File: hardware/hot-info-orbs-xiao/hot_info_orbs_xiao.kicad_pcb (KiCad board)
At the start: 2 copper layers, 198.8 x 28.5 mm, 11 parts, among them SW1 SW_Push, SW2 SW_Push, SW3 SW_Push, U2 ESP32-S3-SuperMini

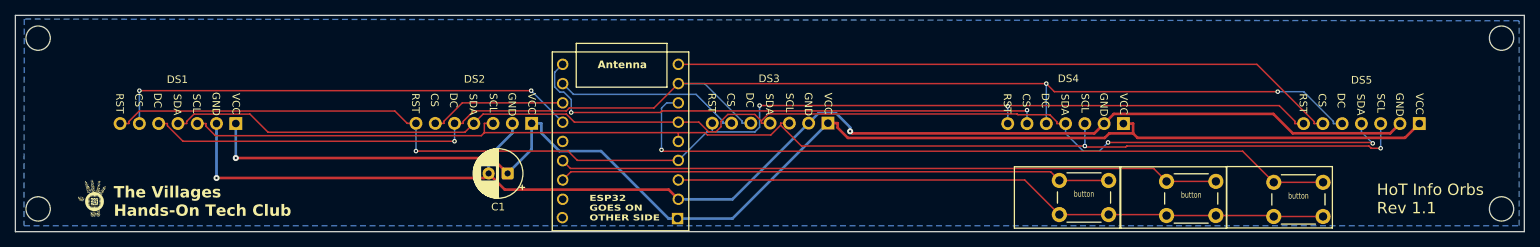
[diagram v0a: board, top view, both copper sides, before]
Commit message: xiao: schematic + PCB swap scripts, first run (WIP checkpoint)
Schematic: SuperMini symbol out, XIAO U2 in with net labels per the pin
map, R1/C2 RC reset on /RST, ERC clean. PCB: XIAO-ESP32-S3-DIP on B.Cu,
R1/C2 on F.Cu, every pad re-netted, tracks ripped. Scripts already carry
the DRC fixes (FPID, Description, 14-pin symbol, U2 y 95, silk) but the
.kicad_sch/.kicad_pcb here are from the run BEFORE those fixes — next
commit reruns both from e6ea813. Committed mid-stream on purpose so a
model switch loses nothing.

Co-Authored-By: Claude Fable 5.1 <noreply@anthropic.com>
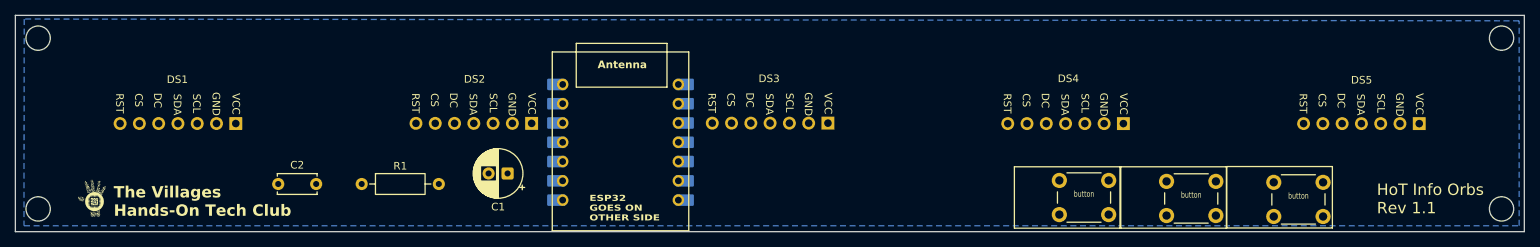
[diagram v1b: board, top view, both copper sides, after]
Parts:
- added C2: 1u, C_Disc_D5.0mm_W2.5mm_P5.00mm, F.Cu at (86.0, 101.5)
- added R1: 10k, R_Axial_DIN0207_L6.3mm_D2.5mm_P10.16mm_Horizontal, F.Cu at (97.0, 101.5)
- U2: value ESP32-S3-SuperMini -> XIAO ESP32-S3 Plus; footprint _ESP32 modules:ESP32S3-SuperMini -> XIAO-ESP32-S3-DIP
- moved U2 0.11 mm to (131.1, 96.0), turned to -90 degrees
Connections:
- DS1 pad 3: Net-(DS1-SCL) -> /SCLK
- DS1 pad 4: Net-(DS1-SDA) -> /MOSI
- DS1 pad 5: Net-(DS1-DC) -> /DC
- DS1 pad 6: Net-(DS1-CS) -> /CS1
- DS1 pad 7: Net-(DS1-RST) -> /RST
- DS2 pad 3: Net-(DS1-SCL) -> /SCLK
- DS2 pad 4: Net-(DS1-SDA) -> /MOSI
- DS2 pad 5: Net-(DS1-DC) -> /DC
- DS2 pad 6: Net-(DS2-CS) -> /CS2
- DS2 pad 7: Net-(DS1-RST) -> /RST
- DS3 pad 3: Net-(DS1-SCL) -> /SCLK
- DS3 pad 4: Net-(DS1-SDA) -> /MOSI
- DS3 pad 5: Net-(DS1-DC) -> /DC
- DS3 pad 6: Net-(DS3-CS) -> /CS3
- DS3 pad 7: Net-(DS1-RST) -> /RST
- DS4 pad 3: Net-(DS1-SCL) -> /SCLK
- DS4 pad 4: Net-(DS1-SDA) -> /MOSI
- DS4 pad 5: Net-(DS1-DC) -> /DC
- DS4 pad 6: Net-(DS4-CS) -> /CS4
- DS4 pad 7: Net-(DS1-RST) -> /RST
- DS5 pad 3: Net-(DS1-SCL) -> /SCLK
- DS5 pad 4: Net-(DS1-SDA) -> /MOSI
- DS5 pad 5: Net-(DS1-DC) -> /DC
- DS5 pad 6: Net-(DS5-CS) -> /CS5
- DS5 pad 7: Net-(DS1-RST) -> /RST
- SW1 pad 1: Net-(U2-GPIO_1) -> /SW1
- SW1 pad 2: Net-(U2-3V3) -> /3V3
- SW2 pad 1: Net-(U2-GPIO_2) -> /SW2
- SW2 pad 2: Net-(U2-3V3) -> /3V3
- SW3 pad 2: Net-(U2-3V3) -> /3V3
- U2 pad 1: +5V -> /SW1
- U2 pad 10: Net-(DS4-CS) -> /DC
- U2 pad 11: Net-(DS3-CS) -> /MOSI
- U2 pad 12: Net-(DS2-CS) -> /3V3
- U2 pad 13: Net-(DS1-CS) -> GND
- U2 pad 14: unconnected-(U2-GPIO_3-Pad14) -> +5V
- U2 pad 2: GND -> /SW2
- U2 pad 3: Net-(U2-3V3) -> /CS1
- U2 pad 4: Net-(DS1-RST) -> /CS2
- U2 pad 5: Net-(DS1-SCL) -> /CS3
- U2 pad 6: Net-(DS1-SDA) -> /SW3
- U2 pad 7: /SW3 -> /CS4
- U2 pad 8: Net-(DS1-DC) -> /CS5
- U2 pad 9: Net-(DS5-CS) -> /SCLK
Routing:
- net +5V: track 182.2 -> 0.00 mm, vias 1 -> 0
- net GND: track 181.4 -> 0.00 mm, vias 2 -> 0
- net Net-(DS1-DC): track 181.2 -> 0.00 mm, vias 3 -> 0
- net Net-(DS1-SDA): track 171.3 -> 0.00 mm, vias 2 -> 0
- net Net-(DS1-RST): track 171.0 -> 0.00 mm, vias 3 -> 0
- net Net-(DS1-SCL): track 170.2 -> 0.00 mm, vias 2 -> 0
- net /SW3: track 96.9 -> 0.00 mm, vias 1 -> 0
- net Net-(DS5-CS): track 88.3 -> 0.00 mm
- net Net-(U2-GPIO_2): track 87.2 -> 0.00 mm
- net Net-(U2-3V3): track 86.9 -> 0.00 mm
- net Net-(U2-GPIO_1): track 72.9 -> 0.00 mm
- net Net-(DS4-CS): track 70.0 -> 0.00 mm, vias 2 -> 0
- net Net-(DS1-CS): track 61.8 -> 0.00 mm, vias 2 -> 0
- net Net-(DS3-CS): track 24.6 -> 0.00 mm
- net Net-(DS2-CS): track 18.1 -> 0.00 mm

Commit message: xiao: schematic + PCB regenerated from e6ea813, DRC/parity clean before routing
Both swap scripts rerun against the untouched copy so the result is
reproducible rather than hand-patched. Symbol trimmed to the 14 edge pins
(renamed XIAO-ESP32-S3-edge) instead of carrying 11 no_connects that
parity flagged as pad-less. U2 moved to y 95.0 so the 21 mm module stays
inside the 107.8 edge; SuperMini silk art rewritten for the XIAO; the
B.Silk keepout rectangle removed (rule area kept). Description copied
via GetField().SetText() — SetField(FIELD_T_DESCRIPTION) makes a stray
field '5' that printed on silk and produced 134 bogus warnings.

DRC: 0 errors, 0 parity, 45 unconnected (not yet routed), 14 accepted
warnings = Seeed outline over its own castellations.

Co-Authored-By: Claude Fable 5.1 <noreply@anthropic.com>
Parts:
- C2: footprint C_Disc_D5.0mm_W2.5mm_P5.00mm -> Capacitor_THT:C_Disc_D5.0mm_W2.5mm_P5.00mm
- R1: footprint R_Axial_DIN0207_L6.3mm_D2.5mm_P10.16mm_Horizontal -> Resistor_THT:R_Axial_DIN0207_L6.3mm_D2.5mm_P10.16mm_Horizontal
- U2: footprint XIAO-ESP32-S3-DIP -> _ESP32 modules:XIAO-ESP32-S3-DIP
- moved U2 1.00 mm to (131.1, 95.0)
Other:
- board text added: "HoT Info Orbs XIAO X0.1"
- board text added: "XIAO GOES ON OTHER SIDE"
- board text added: "XIAO GOES ON THIS SIDE"
- board text removed: "ESP32 GOES ON OTHER SIDE"
- board text removed: "ESP32 GOES ON THIS SIDE"
- board text removed: "HoT Info Orbs Rev 1.1"

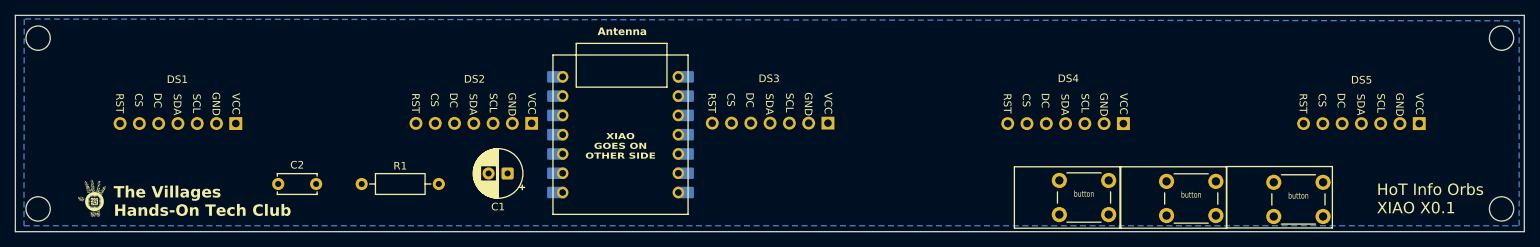
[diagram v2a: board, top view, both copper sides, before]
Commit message: xiao: autorouted, DRC 0 errors / 0 unconnected / parity clean
Freerouting runs headless from tools/route_xiao.py (DSN out, SES in,
DRC with zone refill). Two things had to change for it to finish:

- The GND pour is left out of the DSN. With it, Freerouting treats GND
  as a plane and routes nothing, and the new tracks slice the pour into
  islands (3 starved thermals, 2 unconnected). GND is now routed as
  tracks and the pour is refilled on top.
- Seeed's footprint has two pads per pin (PTH + castellation SMD).
  Freerouting counted the 14 overlaps as violations, stubbed every pin
  and left one net unrouted each run — CS4, then MOSI once CS4 was
  pre-routed by hand, so hand-routing was rejected. merge_xiao_pads.py
  makes each pin one oval THT pad (hole stays at +-7.62, copper to
  +-9.671): 0 violations, 0 unrouted, and one piece of copper for both
  header and castellation builds.

Remaining 14 warnings are Seeed's own silk outline over its pads.
Scripts carry the pcbnew SWIG traps (one board per process, zones
before tracks, GetField not SetField for Description).

Co-Authored-By: Claude Fable 5.1 <noreply@anthropic.com>
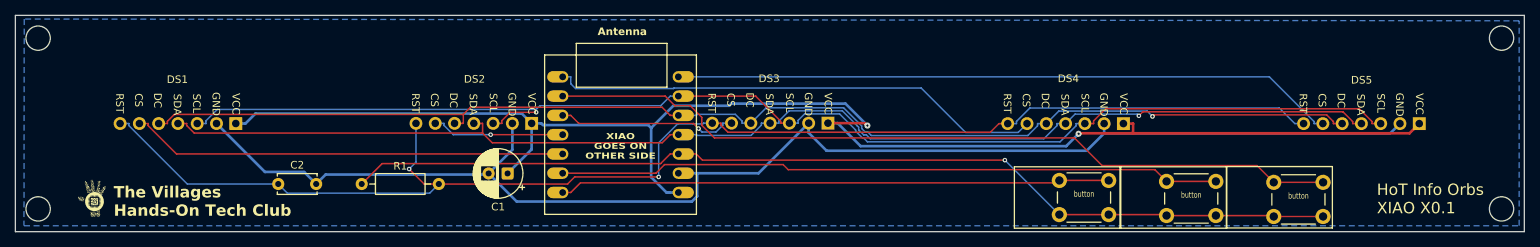
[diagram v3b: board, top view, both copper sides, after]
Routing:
- net +5V: track 0.00 -> 194.2 mm, vias 0 -> 2
- net GND: track 0.00 -> 182.8 mm
- net /RST: track 0.00 -> 180.5 mm, vias 0 -> 2
- net /SCLK: track 0.00 -> 171.6 mm, vias 0 -> 1
- net /MOSI: track 0.00 -> 166.1 mm, vias 0 -> 1
- net /DC: track 0.00 -> 165.5 mm, vias 0 -> 1
- net /3V3: track 0.00 -> 131.7 mm, vias 0 -> 1
- net /SW3: track 0.00 -> 105.5 mm
- net /CS5: track 0.00 -> 87.6 mm
- net /SW2: track 0.00 -> 87.5 mm
- net /SW1: track 0.00 -> 72.6 mm
- net /CS4: track 0.00 -> 65.3 mm
- net /CS1: track 0.00 -> 57.6 mm
- net /CS3: track 0.00 -> 23.8 mm, vias 0 -> 1
- net /CS2: track 0.00 -> 17.6 mm, vias 0 -> 1

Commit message: xiao board: copper-free 40 x 7.5 mm patch for the FPC antenna, SuperMini keepouts removed
The XIAO ESP32-S3 / S3 Plus has a U.FL and a stick-on FPC antenna (Seeed
A-02), not a PCB antenna, so the inherited "Antenna" keepouts and silk were
leftovers. tools/antenna_patch.py replaces them with rule area ANTENNA_PATCH
(no pour/tracks/vias, F.Cu + B.Cu) at x 143.5-183.5, y 99.5-107.0 on the
back right of the XIAO, with a B.Silk box and label. Board re-routed:
0 DRC errors, 0 unconnected, 0 parity, pour has no fill inside the patch.

Why 7.5 mm tall and not the 10.5 mm the strip offers: that strip is the SPI
bus's second channel to DS4/DS5 and the switches. Measured against
Freerouting (20 passes, -mt 1): 10.5 mm -> 3 nets unrouted, 9.0 mm -> CS2
unrouted, 7.5 mm -> clean. Narrowing instead (x from 150 or 155) still left
a net unrouted; x 160.5-183.5 routes at 10.5 mm but is only 23 mm long.
Allowing tracks on F.Cu inside the patch was rejected: copper 1.6 mm behind
a flex antenna still detunes it, and the router does not need the space.

The size is an assumption: Seeed publishes no A-02 dimensions. Measure one
and rerun with PATCH=x0,x1,y0,y1 before ordering boards.

route_xiao.py: -mt 1 (Freerouting 2.4.1 warns its multi-threaded optimizer
is broken) and an assert on SES size - Freerouting writes a 0-byte SES when
nets are left unrouted, and the import then failed with no hint.

Co-Authored-By: Claude Fable 5.1 <noreply@anthropic.com>
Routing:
- net /RST: track 180.5 -> 202.3 mm, vias 2 -> 0
- net /DC: track 165.5 -> 178.5 mm
- net +5V: track 194.2 -> 182.2 mm, vias 2 -> 0
- net /SCLK: track 171.6 -> 181.1 mm, vias 1 -> 2
- net GND: track 182.8 -> 189.8 mm, vias 0 -> 1
- net /MOSI: track 166.1 -> 171.4 mm, vias 1 -> 2
- net /SW1: track 72.6 -> 77.1 mm, vias 0 -> 3
- net /CS2: track 17.6 -> 18.8 mm
- net /3V3: track 131.7 -> 132.3 mm
- net /CS4: track 65.3 -> 64.9 mm, vias 0 -> 1
- net /CS3: track 23.8 -> 23.9 mm, vias 1 -> 0
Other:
- board text added: "STICK FPC ANTENNA HERE no copper under this box"
- board text removed: "Antenna"
